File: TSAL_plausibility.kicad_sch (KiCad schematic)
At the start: 0 parts

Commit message: Changes to Pinout pending
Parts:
- added C13: C_Polarized, Capacitor_SMD:CP_Elec_8x5.4, symbol Device:C_Polarized
- added C14: C, Capacitor_SMD:C_0603_1608Metric, symbol Device:C
- added Q1: NMOS, symbol Simulation_SPICE:NMOS
- added R28, R29, R30, R34, R61, R62, R65, R66: 10k, Resistor_SMD:R_0603_1608Metric, symbol Device:R
- added R31, R32, R33: 3k3, Resistor_SMD:R_0603_1608Metric, symbol Device:R
- added R35: 200R, Resistor_SMD:R_0603_1608Metric, symbol Device:R
- added R63, R64: 33k, Resistor_SMD:R_0603_1608Metric, symbol Device:R
- added U10: SN74HCS266PWR, Package_SO:TSSOP-14_4.4x5mm_P0.65mm, symbol 4xxx_IEEE:4030
- added U12, U9: 74LVC1G32GV, Package_SO:SC-74A-5_1.55x2.9mm_P0.95mm, symbol 4xxx_IEEE:4001
- added U14: OPA355NA, Package_TO_SOT_SMD:SOT-23-6, symbol Amplifier_Operational:OPA355NA
- added U3: 74LVC2G74, Package_SO:TSSOP-8_3x3mm_P0.65mm, symbol 74xGxx:74LVC2G74
- added U6: CD74HC30PWR, Package_SO:TSSOP-14_4.4x5mm_P0.65mm, symbol 4xxx_IEEE:4068
- added U7: 4072, Package_SO:TSSOP-14_4.4x5mm_P0.65mm, symbol 4xxx_IEEE:4072
- added U8: 4001, Package_SO:SC-74A-5_1.55x2.9mm_P0.95mm, symbol 4xxx_IEEE:4001
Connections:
- new net: U7.13, U8.2
- new net: R64.2, R65.1, U14.3 (+)
- new net: C13.1, R63.1, U14.4 (-)
- new net: U7.1, U8.1
- new net: U10.13, U8.4
- new net: R31.2, R34.2, U10.2
- new net: Q1.2 (G), R35.2, R62.2
- new net: U10.10, U6.3 (C), U7.4
- new net: R28.2, U10.1, U10.5, U10.8
- new net: R30.2, R33.2, U10.9
- new net: U10.11, U12.1, U12.2
- new net: R35.1, U9.4
- new net: C14.1, R66.2, U3.6 (~{R})
- new net: R29.2, R32.2, U10.6
- new net: U10.3, U6.1 (A), U7.2
- new net: U10.4, U6.2 (B), U7.3
- new net: U14.1, U3.7 (~{S})
- new net +5V: R61.2, R65.2, R66.1, U10.14 (Vdd), U10.14 (Vdd), U10.14 (Vdd), U10.14 (Vdd), U12.5 (Vdd), U14.5 (ENABLE), U14.6 (V+), U3.8 (VCC), U6.14 (VCC), U7.14 (Vdd), U7.14 (Vdd), U8.5 (Vdd), U9.5 (Vdd)
- new net AIR1: R34.1
- new net AIR1_AUX: U6.4 (D), U7.5
- new net AIR2: R29.1
- new net AIR2_AUX: U6.5 (E), U7.9
- new net GND: C13.2, C14.2, Q1.3 (S), R31.1, R32.1, R33.1, R62.1, R64.1, U10.7 (Vss), U10.7 (Vss), U10.7 (Vss), U10.7 (Vss), U12.3 (Vss), U14.2 (V-), U3.1 (C), U3.2 (D), U3.4 (GND), U6.7 (GND), U7.7 (Vss), U7.7 (Vss), U8.3 (Vss), U9.3 (Vss)
- new net PRCH: R30.1
- new net PRCH_AUX: U6.6 (NC), U7.10
- new net SC: R28.1
- new net TSAL_ERROR: U3.5 (Q), U9.2
- new net TSAL_ERROR_DETECT: R63.2, U12.4
- new net TSAL_GREEN: Q1.1 (D), R61.1
- new net TSAL_OFF: U10.12, U6.8 (Y), U9.1
- new net TS_ON: U6.11 (G), U6.12 (H), U7.11, U7.12
- no-connect marks 0 -> 1
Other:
- note added: "Selection WIP"

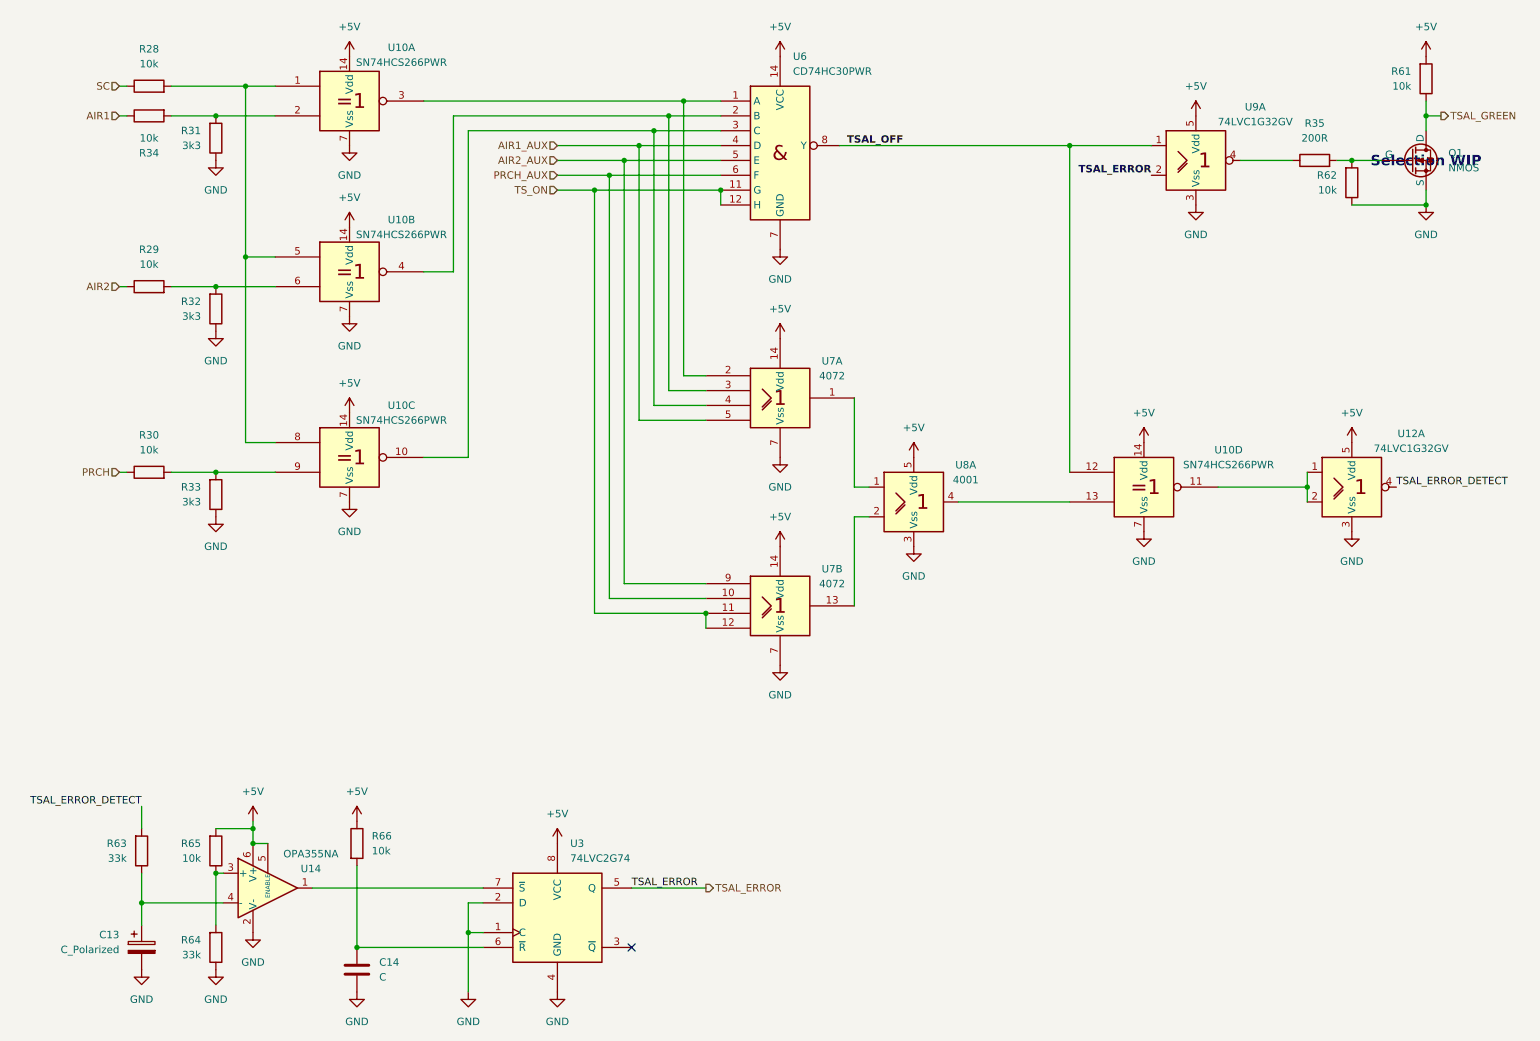
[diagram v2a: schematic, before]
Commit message: Checked Rules. Looks good. Need to fix AIR Aux detection. Need to Fix Coil Activation. Need to add SCS Failure Output and SCS Failure Inhibiter
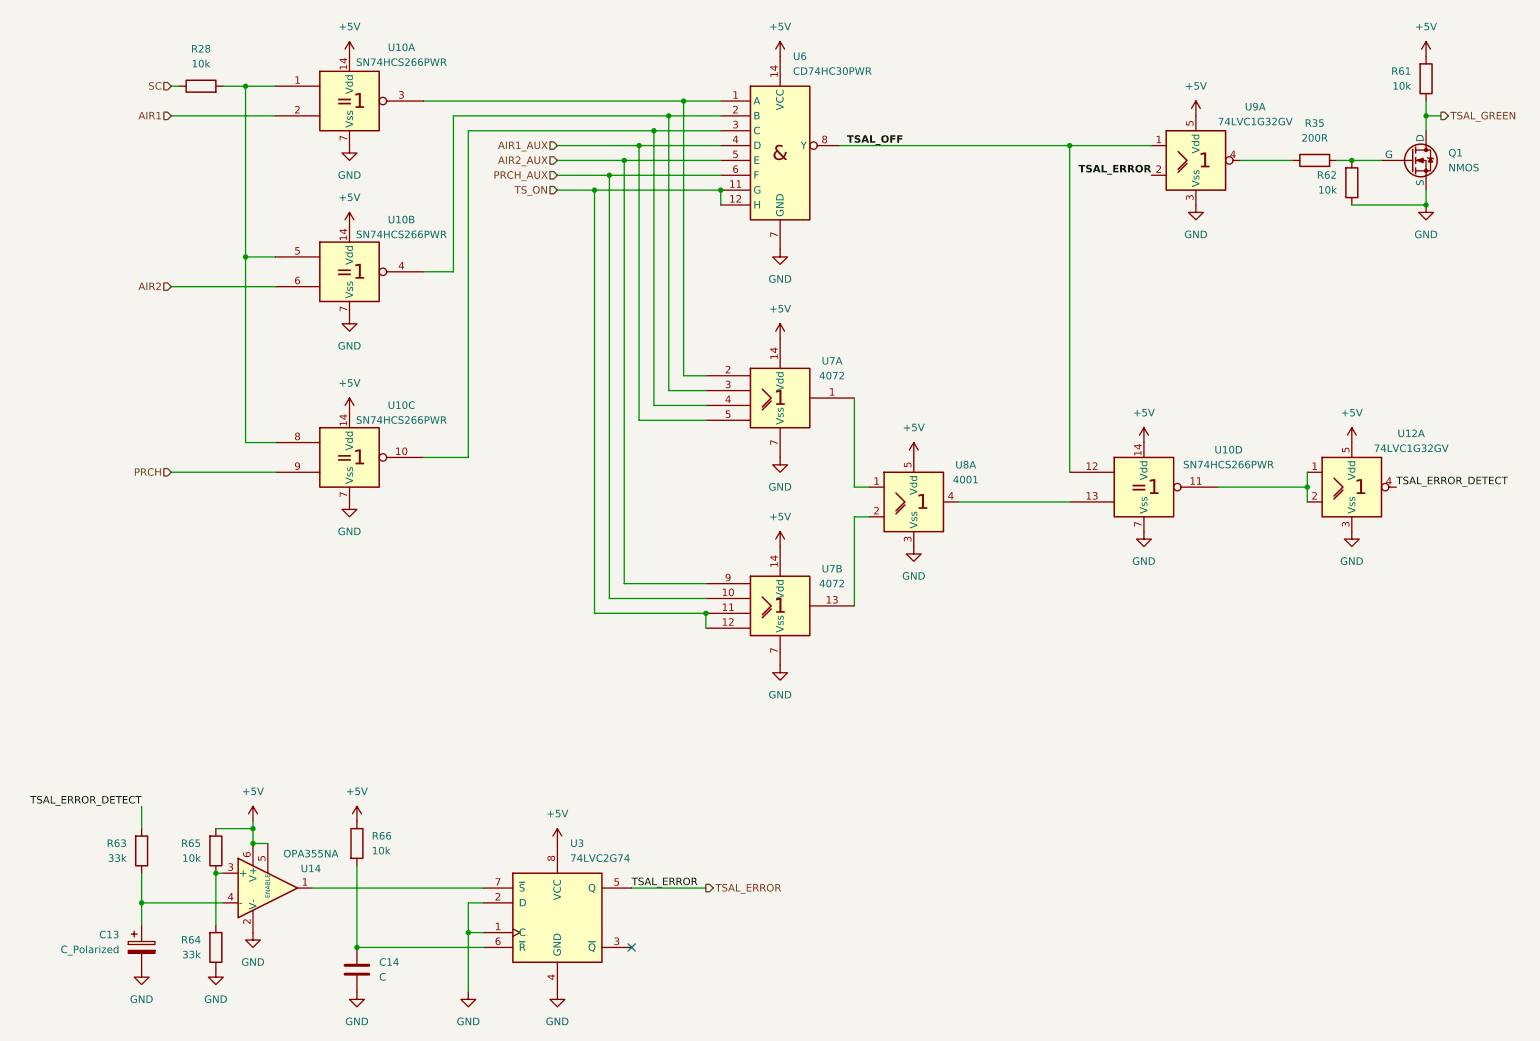
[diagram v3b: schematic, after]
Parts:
- removed R29, R30, R34: 10k, Resistor_SMD:R_0603_1608Metric, symbol Device:R
- removed R31, R32, R33: 3k3, Resistor_SMD:R_0603_1608Metric, symbol Device:R
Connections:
- net AIR1: now also U10.2
- net AIR2: now also U10.6
- net PRCH: now also U10.9
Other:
- note removed: "Selection WIP"
- moved on the sheet: R28

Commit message: Added decoupling Caps
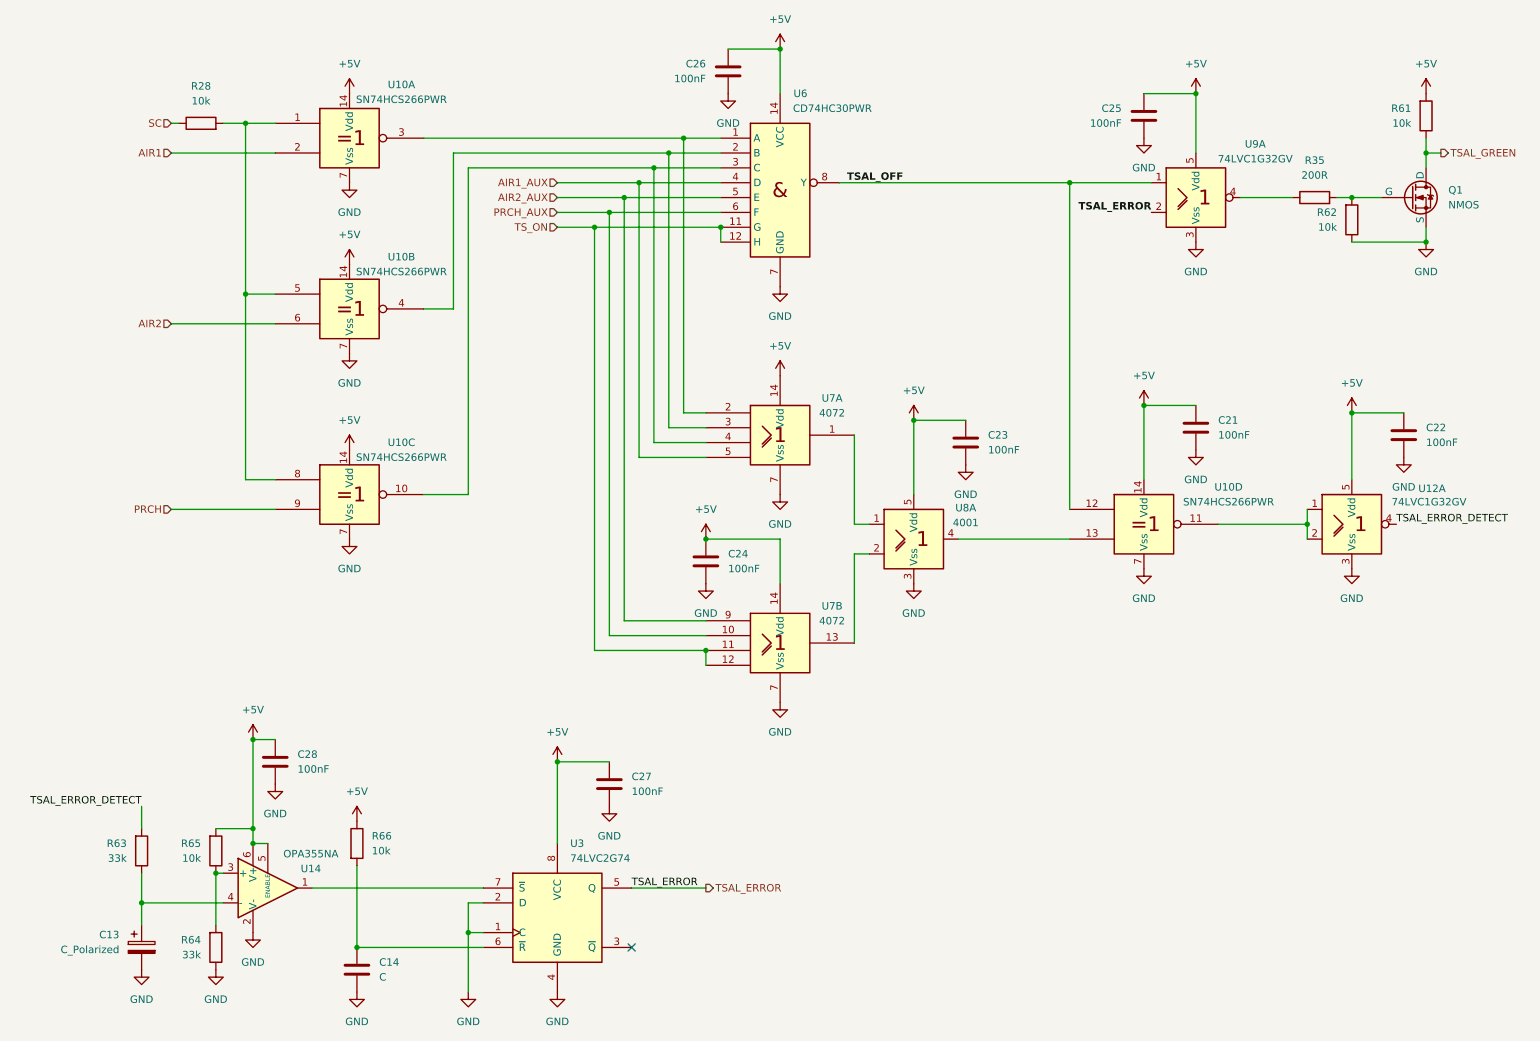
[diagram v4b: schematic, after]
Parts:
- added C21, C22, C23, C24, C25, C26, C27, C28: 100nF, symbol Device:C
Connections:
- net +5V: now also C21.1, C22.1, C23.1, C24.1, C25.1, C26.1, C27.1, C28.1
- net GND: now also C21.2, C22.2, C23.2, C24.2, C25.2, C26.2, C27.2, C28.2
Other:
- moved on the sheet: Q1, R28, R35, R61, R62, U10A, U10B, U10C, U10D, U12A, U6, U7A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

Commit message: Added Rules
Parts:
- added R84, R87: 30k, symbol Device:R
- added R88, R89, R90: 7k5, symbol Device:R
- R28: value 10k -> 30k; footprint Resistor_SMD:R_0603_1608Metric -> (none)
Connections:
- net +5V: no longer R61.2
- net AIR1: now also R28.1; no longer U10.2
- net AIR2: now also R84.1; no longer U10.6
- net GND: now also R88.1, R89.1, R90.1
- net PRCH: now also R87.1; no longer U10.9
- net SC: now also U10.1, U10.5, U10.8; no longer R28.1
- new net: R28.2, R88.2, U10.2
- new net: R87.2, R90.2, U10.9
- new net: R84.2, R89.2, U10.6
- new net +24V: R61.2

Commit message: Submission Ready. ESF 15.07.24
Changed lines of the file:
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@@
 			(font
 				(size 1.27 1.27)
+				(bold yes)
 			)
 			(justify left bottom)
@@
 			(font
 				(size 1.27 1.27)
-				(bold yes)
 			)
 			(justify left bottom)

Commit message: ⠀⠀⠀⠀⠀⠀⠀⠀⠀⠀⠀⠀⠀⠀⠀⠀⠀⠀⠀⠀⠀⠀⠀⠀⠀⠀⠀⠀⠀⠀⠀⠀⠀⠀⠀⠀⠀⣠⣤⣤⣤⡀⠀⠀⠀⠀⠀⠀⠀⠀⠀⠀⠀⠀⠀⠀⠀⠀⠀⠀⠀⠀⠀⠀⠀ ⠀⠀⠀⠀⠀⠀⠀⠀⠀⠀⠀⠀⠀⠀⠀⠀⠀⠀⠀⠀⠀⠀⠀⠀⠀⠀⠀⠀⠀⠀⠀⠀⠀⠀⣠⣶⣿⠟⠉⠉⠻⣿⡄⠀⠀⠀⠀⠀⠀⠀⠀⠀⠀⠀⠀⠀⠀⠀⠀⠀⠀⠀⠀⠀⠀ ⠀⠀⠀⠀⠀⠀⠀⠀⠀⠀⠀⠀⠀⠀⠀⠀⠀⠀⠀⠀⠀⠀⠀⠀⠀⠀⠀⠀⠀⠀⠀⢀⣤⣾⠿⠉⠀⠀⠀⠀⠀⠹⣿⡄⠀⠀⠀⠀⠀⠀⠀⠀⠀⠀⠀⠀⠀⠀⠀⠀⠀⠀⣀⣴⣾ ⠀⠀⠀⠀⠀⠀⠀⠀⠀⠀⠀⠀⠀⠀⠀⠀⠀⠀⠀⠀⠀⠀⠀⠀⠀⠀⠀⠀⠀⢀⣴⣿⠟⠁⠀⠀⠀⠀⠀⠀⠀⠀⣿⣿⠀⠀⠀⠀⠀⠀⠀⠀⠀⠀⠀⠀⠀⠀⠀⣀⣴⣾⡿⠛⠉ ⠀⠀⠀⠀⠀⠀⠀⠀⠀⠀⠀⠀⠀⠀⠀⠀⠀⠀⠀⠀⠀⠀⠀⠀⠀⠀⠀⢀⣴⣿⠟⠁⠀⠀⠀⠀⠀⠀⠀⠀⠀⠀⢸⣿⡆⠀⠀⠀⠀⠀⠀⠀⠀⠀⠀⠀⢀⣴⣾⡿⠟⠁⠀⠀⠀ ⠀⠀⠀⠀⠀⠀⠀⠀⠀⠀⠀⠀⠀⠀⠀⠀⠀⠀⠀⠀⠀⠀⠀⠀⢀⣀⣴⣿⡿⠃⠀⠀⠀⠀⠀⠀⠀⠀⠀⠀⠀⠀⢸⣿⣷⣶⣶⣦⣤⣤⣄⡀⠀⢀⣠⣾⣿⠿⠋⠀⠀⠀⠀⠀⣠ ⠀⠀⠀⠀⠀⠀⠀⠀⠀⠀⠀⠀⠀⠀⠀⠀⠀⠀⠀⠀⠀⠀⠀⣼⣿⣿⡿⠋⠀⠀⠀⠀⠀⠀⠀⠀⠀⠀⠀⣠⣤⠶⠞⣿⠟⠋⠉⠉⠙⣻⠿⢿⣿⣿⣿⠟⠁⠀⠀⠀⠀⠀⢀⡼⠁ ⠀⠀⠀⠀⠀⠀⠀⠀⠀⠀⠀⠀⠀⠀⠀⠀⠀⠀⠀⠀⠀⠀⢰⣿⠁⠛⠀⠀⠀⠀⠀⠀⠀⠀⠀⠀⠀⠀⣰⠟⠁⢠⡞⠁⠀⠀⠀⢀⡴⠋⠀⢀⡿⠋⠁⠀⠀⠀⠀⠀⠀⠀⡞⠁⠀ ⠀⠀⠀⠀⠀⠀⠀⠀⠀⠀⠀⠀⠀⠀⠀⠀⠀⠀⠀⠀⠀⣠⣼⣿⡄⠀⠀⠀⠀⠀⠀⠀⠀⠀⠀⠀⠀⣼⠃⠀⢠⠏⠀⠀⠀⠀⣰⠏⠀⠀⣠⠟⠀⠀⠀⠀⠀⠀⠀⠀⠀⢸⡥⠤⡀ ⠀⠀⠀⠀⠀⠀⠀⠀⠀⠀⠀⠀⠀⠀⠀⠀⠀⠀⠀⠀⣰⣿⠟⠁⠀⠀⠀⠀⠀⠀⠀⠀⠀⠀⠀⠀⠠⣇⠀⣠⡏⠀⠀⠀⠀⣼⠁⠀⠀⣰⠋⠀⠀⠀⠀⠀⠀⠀⠀⠀⠀⠀⢀⡴⠁ ⠀⠀⠀⠀⠀⠀⠀⠀⠀⠀⠀⠀⠀⠀⠀⠀⣀⣄⣄⣼⣿⠋⠀⠀⠀⠀⠀⠀⠀⠀⠀⠀⠀⠀⠀⠀⠀⢻⡶⠋⠀⠀⠀⠀⢸⣧⠀⠀⣴⠃⠀⠀⠀⠀⠀⠀⠀⠀⠀⠀⠀⠀⠘⢧⠀ ⠀⠀⠀⠀⠀⠀⠀⠀⢀⣀⣀⠀⠀⠀⠀⣾⡿⠿⣿⡿⠁⠀⠀⠀⠀⠀⠀⣠⣶⣶⣶⡀⠀⠀⠀⠀⠀⠀⠀⠀⠀⠀⠀⠀⠀⠙⠛⠛⠁⠀⠀⠀⠀⠀⠀⠀⠀⠀⠀⠀⠀⠀⠀⠈⠳ ⠀⠀⠀⠀⠀⠀⢀⣾⠿⠛⢿⣿⣷⣄⡀⣿⠃⠀⠈⠀⠀⠀⠀⠀⠀⢀⣾⣿⣿⣿⣿⣧⠀⠀⠀⠀⠀⠀⠀⠀⠀⠀⠀⠀⠀⠀⠀⠀⠀⠀⠀⠀⠀⠀⠀⠀⠀⠀⠀⠀⠀⠀⠀⠀⠀ ⠀⠀⠀⣠⣤⣦⣼⣿⠀⠀⠀⣿⣿⣿⣿⣿⣦⣀⠀⠀⠀⠀⠀⠀⠀⣿⣿⣿⣿⣿⣿⡿⠀⠀⠀⢀⣀⣀⣀⣀⡀⠀⠀⠀⠀⠀⠀⠀⠀⠀⠀⣤⣾⣿⣿⣿⣷⣄⠀⠀⠀⠀⠀⠀⠀ ⠀⣠⣾⡿⠋⠉⠉⠁⠀⠀⠀⠀⠉⢯⡙⠻⣿⣿⣷⣤⡀⠀⠀⠀⠀⢿⣿⣿⣿⣿⡿⠃⢀⡤⠖⠋⠉⠉⠉⠉⠉⠉⠒⠦⣄⠀⠀⠀⠀⠀⣾⣿⣿⣿⣿⣿⣿⣿⣧⠀⠀⠀⠀⠀⠀ ⣾⣿⠋⠀⠀⠀⠀⣀⣀⠀⠀⠀⠀⠀⠙⢦⣄⠉⠻⢿⣿⣷⣦⡀⠀⠈⠙⠛⠛⠋⠀⢰⠟⡇⠀⠀⠀⠀⠀⠀⠀⠀⠀⠀⠈⠳⣄⠀⠀⠀⣿⣿⣿⣿⣿⣿⣿⣿⣿⠀⠀⠀⠀⠀⠀ ⣿⡇⠀⠀⠀⣴⠟⣫⣿⣿⣄⠀⠀⠀⠀⡶⢌⡙⠶⣤⡈⠛⠿⣿⣷⣦⣀⠀⠀⠀⠀⡇⠀⢻⣄⠀⠀⣠⢷⠀⠀⠀⠀⠀⡶⠀⠘⡆⠀⠀⠻⣿⣿⣿⣿⣿⣿⣿⡟⠀⠀⠀⠀⠀⠀ ⣿⡇⠀⠀⢸⣟⢸⣿⣿⣿⣿⠀⠀⠀⠀⡇⠀⠈⠛⠦⣝⡳⢤⣈⠛⠻⣿⣷⣦⣀⠀⠀⠀⠀⠈⠙⠋⠁⠀⠛⠦⠤⠤⠚⠁⠀⠀⢳⠀⠀⠀⠈⠛⠿⠿⠿⠟⠋⠀⠀⠀⠀⠀⠀⠀ ⣿⡇⠀⠀⠈⢿⣞⣿⣿⣿⠏⠀⠀⠀⠀⡇⠀⠀⠀⠀⠀⠙⠳⢬⣛⠦⠀⠙⢻⣿⣷⣦⣀⠀⠀⠀⠀⠀⠀⠀⠀⠀⠀⠀⠀⠀⠀⡞⠀⠀⠀⠀⠀⠀⠀⠀⠀⠀⠀⠀⠀⠀⠀⠀⠀ ⣿⡇⠀⠀⠀⠀⠉⠛⠋⠁⠀⠀⠀⠀⠀⡇⠀⠀⠀⠀⠀⠀⠀⠀⠈⠁⠀⠀⠈⣿⠉⢻⣿⣷⣦⣀⠀⠀⠀⠀⠀⠀⠀⠀⠀⢀⡼⠁⠀⠀⠀⠀⠀⠀⠀⠀⠀⠀⠀⠀⠀⠀⠀⠀⠀ ⣿⡇⠀⠀⠀⠀⠀⣠⣄⠀⠀⢰⠶⠒⠒⢧⣄⡀⠀⠀⠀⠀⠀⠀⠀⠀⠀⠀⠀⣿⠀⢸⡇⢸⡟⢿⣷⣦⣴⣶⣶⣶⣶⣤⣔⠋⠀⠀⠀⠀⠀⠀⠀⠀⠀⠀⠀⠀⠀⠀⠀⠀⠀⠀⠀ ⣿⡇⠀⠀⣤⠀⠀⠿⠿⠁⢀⡿⠀⠀⠀⡄⠈⠙⡷⢦⣄⡀⠀⠀⠀⠀⠀⠀⠀⣿⠀⢸⡇⢸⡇⠀⣿⠙⣿⣿⣉⠉⠙⠿⣿⣧⠀⠀⠀⠀⠀⠀⠀⠀⠀⠀⠀⠀⠀⠀⠀⠀⠀⠀⠀ ⣿⡇⠀⠀⠙⠷⢤⣀⣠⠴⠛⠁⠀⠀⠀⠇⠀⠀⡇⢸⡏⢹⡷⢦⣄⡀⠀⠀⠀⣿⡀⢸⡇⢸⡇⠀⡟⠀⢸⠀⢹⡷⢦⣄⣘⣿⡆⠀⠀⠀⠀⠀⠀⠀⠀⠀⠀⠀⠀⠀⠀⠀⠀⠀⠀ ⣿⣿⠢⣤⡀⠀⠀⠀⠀⠀⠀⣠⠾⣿⣿⡷⣤⣀⡇⠸⡇⢸⡇⢸⠉⠙⠳⢦⣄⡻⢿⣾⣧⣸⣧⠀⡇⠀⢸⠀⢸⡇⢤⣈⠙⠻⣿⣆⠀⠀⠀⠀⠀⠀⠀⠀⠀⠀⠀⠀⠀⠀⠀⠀⠀ ⢹⣿⣷⣌⡉⠛⠲⢶⣶⠖⠛⠛⢶⣄⡉⠛⠿⣽⣿⣶⣧⣸⡇⢸⠀⠀⠀⠀⠈⠙⠲⢮⣝⠻⣿⣷⣷⣄⣸⠀⢸⡇⠀⠈⠁⠀⢸⣿⠀⠀⠀⠀⠀⠀⠀⠀⠀⠀⠀⠀⠀⠀⠀⠀⠀ ⠀⠈⠙⠻⢿⣷⣶⣤⣉⡻⢶⣄⣀⠈⠙⠳⢦⣈⡉⠻⢿⣿⣷⣾⣦⡀⠀⠀⠀⠀⠀⠀⠈⠙⠲⢭⣛⠿⣿⣷⣼⡇⠀⠀⠀⠀⠈⣿⡇⠀⠀⠀⠀⠀⠀⣀⠀⠀⠀⠀⠀⠀⠀⠀⣀ ⠀⠀⠀⠀⠀⠈⠙⠻⢿⣿⣷⣶⣽⣻⡦⠀⠀⠈⠙⠷⣦⣌⡙⠻⢿⣟⣷⣤⣀⠀⠀⠀⠀⠀⠀⠀⠈⠙⠳⢯⣻⡇⠀⠀⠀⠀⠀⢸⣿⠀⣀⠀⠀⠀⠀⠈⠳⣄⠀⠀⠀⢀⡏⠙⠛ ⠀⠀⠀⠀⠀⠀⠀⠀⠀⠈⠛⠻⢿⣿⣿⣿⣶⣤⣤⣤⣀⣈⠛⠷⣤⣈⡛⠷⢽⡻⢶⣄⣀⠀⠀⠀⠀⠀⠀⠀⠈⠛⠳⢤⣀⠀⠀⢸⣿⡀⠈⠳⢤⣀⣀⣰⠃⠈⠛⠶⠶⠿⠃⠀⠀ ⠀⠀⠀⠀⠀⠀⠀⠀⠀⠀⠀⠀⠀⢈⣿⡿⠛⠉⠙⠛⠛⠻⢷⣦⣄⣩⣿⠶⠖⠛⠛⠛⠛⠛⠛⠿⢷⣶⣦⣄⠀⠀⠀⠀⠉⢻⣶⣿⣿⠇⠀⠀⠀⠉⠉⠀⠀⠀⠀⠀⠀⠀⠀⠀⠀ ⠀⠀⠀⠀⠀⠀⠀⠀⠀⠀⠀⠀⠀⣼⣿⠁⠀⠀⠀⠀⠀⠀⠀⣿⣿⠋⠀⠀⠀⠀⠀⣠⠖⠂⠀⠀⠀⠈⠙⠿⣿⣦⡄⠀⠀⣸⣿⠟⠋⠀⠀⠀⠀⠀⠀⠀⠀⠀⠀⠀⠀⠀⠀⠀⠀ ⠀⠀⠀⠀⠀⠀⠀⠀⠀⠀⠀⠀⢰⣿⡟⠀⠀⠀⠀⠀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
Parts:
- C21, C22, C23, C24, C25, C26, C27, C28: footprint (none) -> Capacitor_SMD:C_0603_1608Metric
- Q1: footprint (none) -> Package_TO_SOT_SMD:SOT-23-3
- R28, R84, R87, R88, R89, R90: footprint (none) -> Resistor_SMD:R_0603_1608Metric
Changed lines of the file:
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@@
 			)
 		)
-		(property "Footprint" ""
+		(property "Footprint" "Capacitor_SMD:C_0603_1608Metric"
 			(at 229.5652 87.63 0)
 			(effects
@@
 			)
 		)
-		(property "Footprint" ""
+		(property "Footprint" "Capacitor_SMD:C_0603_1608Metric"
 			(at 218.7448 34.29 0)
 			(effects
@@
 			)
 		)
-		(property "Footprint" ""
+		(property "Footprint" "Capacitor_SMD:C_0603_1608Metric"
 			(at 72.0852 144.78 0)
 			(effects
@@
 			)
 		)
-		(property "Footprint" ""
+		(property "Footprint" "Resistor_SMD:R_0603_1608Metric"
 			(at 52.578 40.64 90)
 			(effects
@@
 			)
 		)
-		(property "Footprint" ""
+		(property "Footprint" "Capacitor_SMD:C_0603_1608Metric"
 			(at 129.2352 148.59 0)
 			(effects
@@
 			)
 		)
-		(property "Footprint" ""
+		(property "Footprint" "Package_TO_SOT_SMD:SOT-23-3"
 			(at 270.51 41.91 0)
 			(effects
@@
 			)
 		)
-		(property "Footprint" ""
+		(property "Footprint" "Resistor_SMD:R_0603_1608Metric"
 			(at 44.45 99.568 90)
 			(effects
@@
 			)
 		)
-		(property "Footprint" ""
+		(property "Footprint" "Resistor_SMD:R_0603_1608Metric"
 			(at 52.578 69.85 90)
 			(effects
@@
 			)
 		)
-		(property "Footprint" ""
+		(property "Footprint" "Capacitor_SMD:C_0603_1608Metric"
 			(at 147.6248 26.67 0)
 			(effects
@@
 			)
 		)
-		(property "Footprint" ""
+		(property "Footprint" "Resistor_SMD:R_0603_1608Metric"
 			(at 52.578 101.6 90)
 			(effects
@@
 			)
 		)
-		(property "Footprint" ""
+		(property "Footprint" "Resistor_SMD:R_0603_1608Metric"
 			(at 44.45 38.608 90)
 			(effects
@@
 			)
 		)
-		(property "Footprint" ""
+		(property "Footprint" "Resistor_SMD:R_0603_1608Metric"
 			(at 44.45 67.818 90)
 			(effects
@@
 			)
 		)
-		(property "Footprint" ""
+		(property "Footprint" "Capacitor_SMD:C_0603_1608Metric"
 			(at 265.1252 88.9 0)
 			(effects
@@
 			)
 		)
-		(property "Footprint" ""
+		(property "Footprint" "Capacitor_SMD:C_0603_1608Metric"
 			(at 145.7452 110.49 0)
 			(effects
@@
 			)
 		)
-		(property "Footprint" ""
+		(property "Footprint" "Capacitor_SMD:C_0603_1608Metric"
 			(at 190.1952 90.17 0)
 			(effects

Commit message: Misc.
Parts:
- Q1: Mouser (none) -> 726-BSS316NH6327
- R88, R89, R90: value 7k5 -> e
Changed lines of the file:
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@@
 			)
 		)
-		(property "Value" "7k5"
+		(property "Value" "e"
 			(at 53.34 41.9099 0)
 			(effects
@@
 		(property "Sim.Pins" "1=D 2=G 3=S"
 			(at 265.43 59.69 0)
+			(effects
+				(font
+					(size 1.27 1.27)
+				)
+				(hide yes)
+			)
+		)
+		(property "Mouser" "726-BSS316NH6327"
+			(at 265.43 44.45 0)
 			(effects
 				(font
@@
 			)
 		)
-		(property "Value" "7k5"
+		(property "Value" "e"
 			(at 53.34 71.1199 0)
 			(effects
@@
 			)
 		)
-		(property "Value" "7k5"
+		(property "Value" "e"
 			(at 53.34 102.8699 0)
 			(effects
